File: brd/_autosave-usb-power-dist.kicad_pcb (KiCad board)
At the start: 2 copper layers, 50 x 50 mm, 40 parts, among them J1 POWER IN, J2 USB_A, J3 USB_A, J4 CASC IN, J5 CASC OUT, U1 TPS2552D, U2 TPS2552D, U3 TPS2513

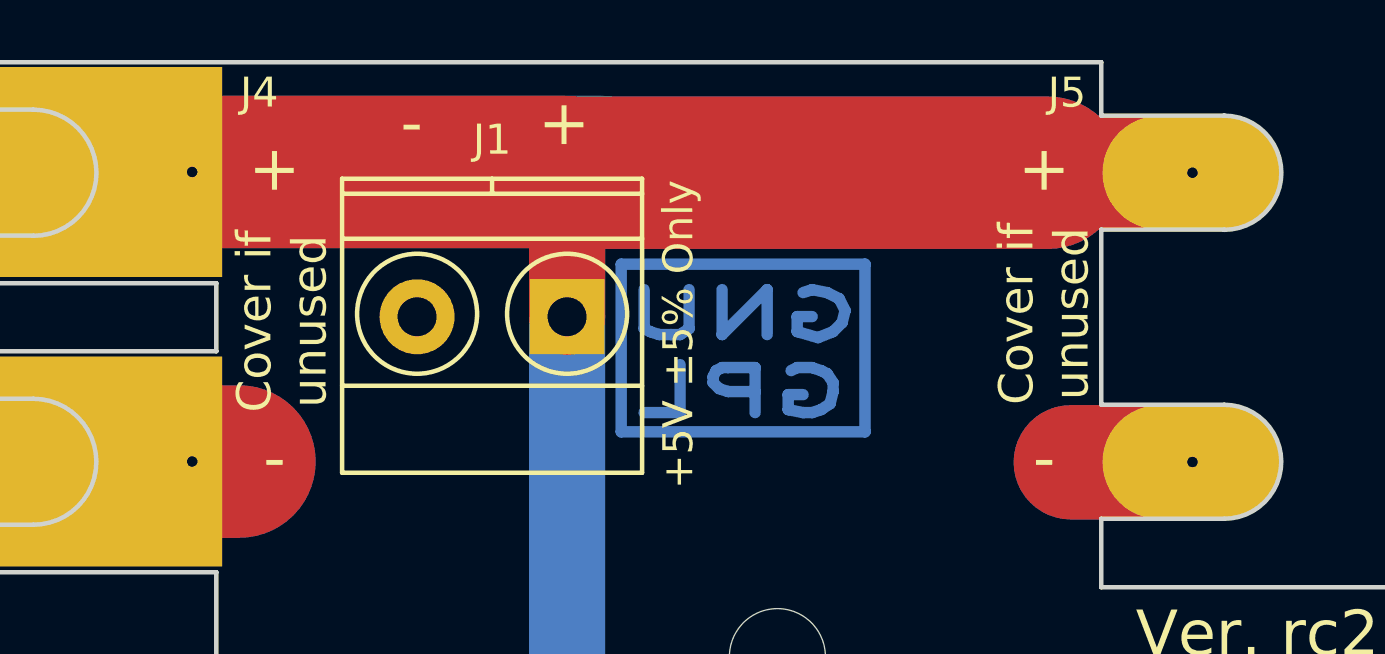
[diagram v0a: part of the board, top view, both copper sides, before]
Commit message: corregido fallo ausencia de pista pin ¬FAULT
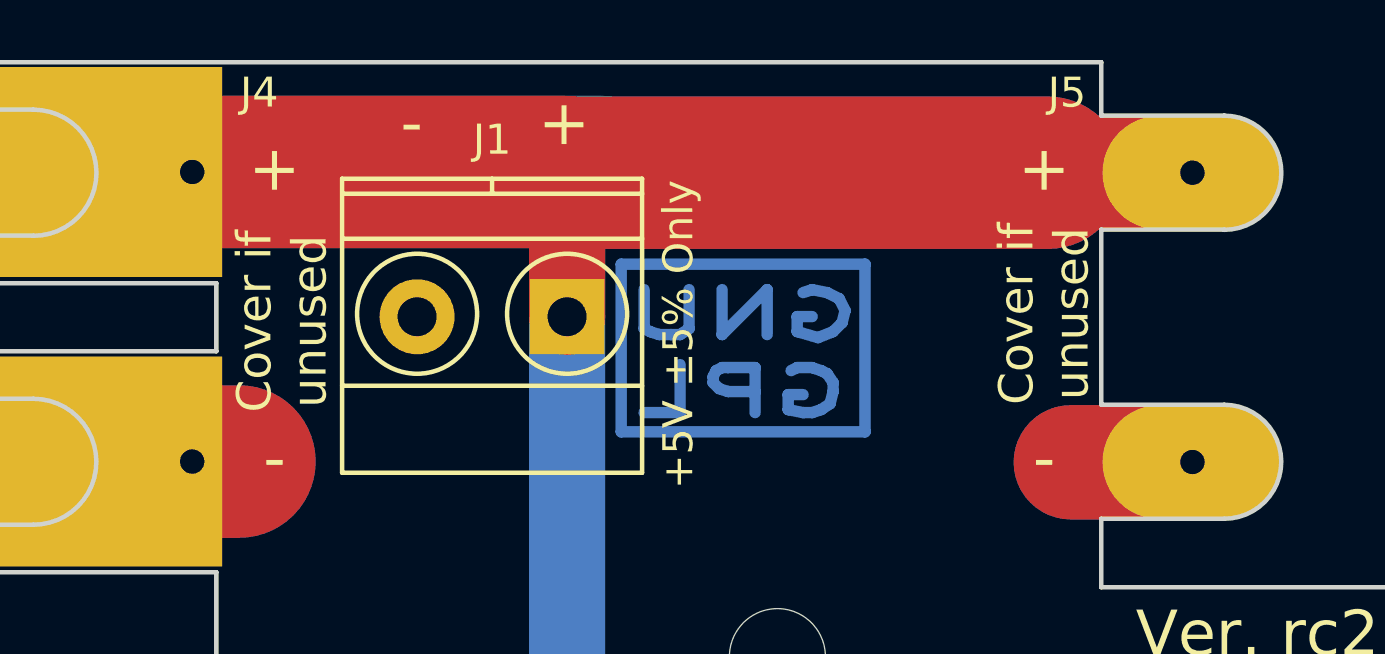
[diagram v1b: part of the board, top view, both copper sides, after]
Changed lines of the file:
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@@
-(kicad_pcb (version 4) (host pcbnew 4.0.6-e0-6349~53~ubuntu16.04.1)
+(kicad_pcb (version 4) (host pcbnew 4.0.7-e2-6376~58~ubuntu16.04.1)
   (general
     (links 74)
-    (no_connects 5)
-    (area 101.330001 62.705 205.957143 139.733001)
+    (no_connects 2)
+    (area 122.860999 80.950999 173.011001 131.101001)
     (thickness 1.6)
     (drawings 77)
@@
     (mod_text_size 1 1)
     (mod_text_width 0.15)
-    (pad_size 3.8 6)
-    (pad_drill 0.35)
+    (pad_size 7 10)
+    (pad_drill 0.8128)
     (pad_to_mask_clearance 0.2)
     (aux_axis_origin 0 0)
@@
     (fp_line (start -2.6162 -4.1148) (end -2.1336 -5.1816) (layer Cmts.User) (width 0.381))
     (fp_line (start -2.1336 -5.1816) (end -2.1336 -3.6322) (layer Cmts.User) (width 0.381))
-    (pad 1 thru_hole rect (at 0.508 0.127 270) (size 7 10) (drill 0.35 (offset 0 4)) (layers *.Cu *.Mask)
+    (pad 1 thru_hole rect (at 0.508 0.127 270) (size 7 10) (drill 0.8128 (offset 0 4)) (layers *.Cu *.Mask)
       (net 1 +5V))
-    (pad 2 thru_hole rect (at 10.16 0.127 270) (size 7 10) (drill 0.35 (offset 0 4)) (layers *.Cu *.Mask)
+    (pad 2 thru_hole rect (at 10.16 0.127 270) (size 7 10) (drill 0.8128 (offset 0 4)) (layers *.Cu *.Mask)
       (net 2 GND))
   )
@@
     (fp_line (start -2.6162 -4.1148) (end -2.1336 -5.1816) (layer Cmts.User) (width 0.381))
     (fp_line (start -2.1336 -5.1816) (end -2.1336 -3.6322) (layer Cmts.User) (width 0.381))
-    (pad 1 thru_hole oval (at 0 1.532 270) (size 3.8 6) (drill 0.35) (layers *.Cu *.Mask)
+    (pad 1 thru_hole oval (at 0 1.532 270) (size 3.8 6) (drill 0.8128) (layers *.Cu *.Mask)
       (net 1 +5V))
-    (pad 2 thru_hole oval (at 9.643 1.532 270) (size 3.8 6) (drill 0.35) (layers *.Cu *.Mask)
-      (net 2 GND))
-  )
+    (pad 2 thru_hole oval (at 9.643 1.532 270) (size 3.8 6) (drill 0.8128) (layers *.Cu *.Mask)
+      (net 2 GND))
+  )
